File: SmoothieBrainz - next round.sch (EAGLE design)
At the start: 232 parts, among them IC1 LPC1769, IC7 74LVC1G04, Q1 BSL207SP, Q2 12MHz, SW1 SW_TACT_4P_B, SW3 SW_TACT_4P_B, T1 BC817, U3 USD-SOCKETUSD, X1 MSTBA2, X14 USBPTH, X2 GMSTBA2, X3 GMSTBA4, X4 1751248, X5 1751248, X6 1751248, X7 1751248

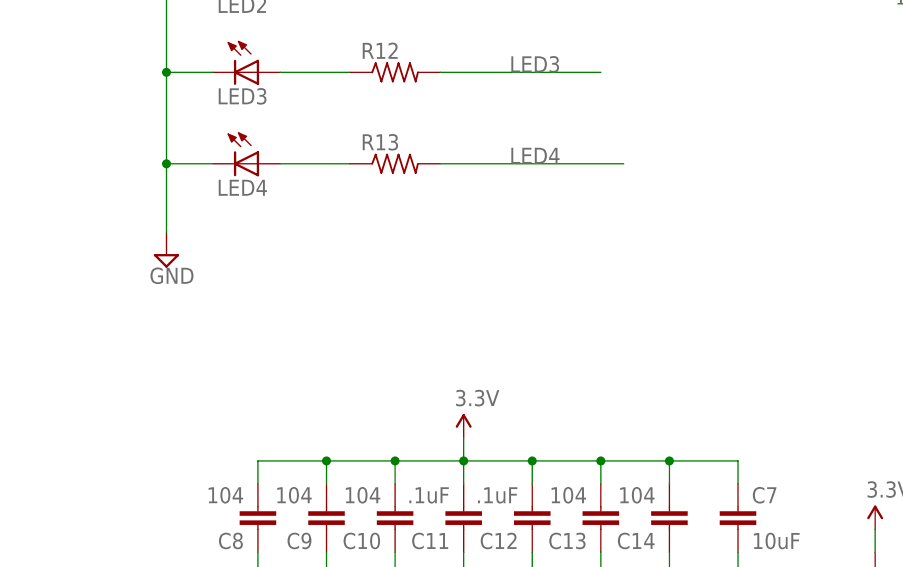
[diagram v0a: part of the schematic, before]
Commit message: Added VMOT indicator led
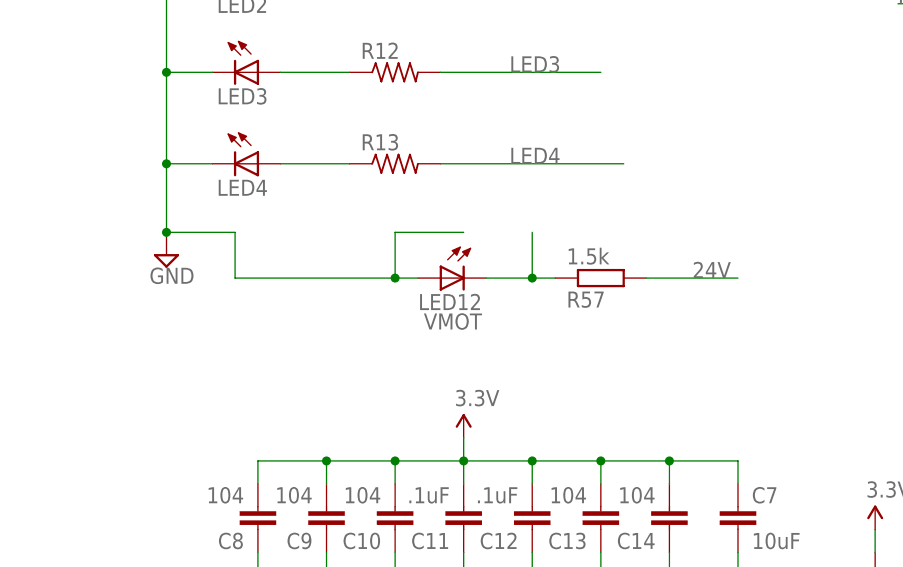
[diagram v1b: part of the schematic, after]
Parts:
- added LED12: VMOT, led:LEDSML0603
- added R57: 1.5k, resistor:R-EU_R0603
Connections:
- new net N$23: LED12.C, R57.1
- net 24V: now also R57.2
- net GND: now also LED12.A
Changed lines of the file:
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@@
 <part name="C23" library="resistor" deviceset="CPOL-EU" device="153CLV-0605" value="100u"/>
 <part name="C24" library="resistor" deviceset="CPOL-EU" device="153CLV-0605" value="100u"/>
+<part name="LED12" library="led" deviceset="LED" device="SML0603" value="VMOT"/>
+<part name="R57" library="resistor" deviceset="R-EU_" device="R0603" value="1.5k"/>
 </parts>
 <sheets>
@@
 <instance part="C23" gate="G$1" x="20.32" y="7.62"/>
 <instance part="C24" gate="G$1" x="68.58" y="7.62"/>
+<instance part="LED12" gate="G$1" x="43.18" y="73.66" rot="MR270"/>
+<instance part="R57" gate="G$1" x="60.96" y="73.66" rot="MR180"/>
 </instances>
 <busses>
@@
 <pinref part="LED3" gate="G$1" pin="C"/>
 <pinref part="LED4" gate="G$1" pin="C"/>
+<wire x1="12.7" y1="78.74" x2="20.32" y2="78.74" width="0.1524" layer="91"/>
+<wire x1="20.32" y1="78.74" x2="20.32" y2="73.66" width="0.1524" layer="91"/>
+<junction x="12.7" y="78.74"/>
+<pinref part="LED12" gate="G$1" pin="A"/>
+<wire x1="20.32" y1="73.66" x2="38.1" y2="73.66" width="0.1524" layer="91"/>
+<wire x1="38.1" y1="73.66" x2="40.64" y2="73.66" width="0.1524" layer="91"/>
+<wire x1="45.72" y1="78.74" x2="38.1" y2="78.74" width="0.1524" layer="91"/>
+<wire x1="38.1" y1="78.74" x2="38.1" y2="73.66" width="0.1524" layer="91"/>
+<junction x="38.1" y="73.66"/>
 </segment>
 <segment>
@@
 <label x="121.92" y="307.34" size="1.778" layer="95"/>
 </segment>
+<segment>
+<pinref part="R57" gate="G$1" pin="2"/>
+<wire x1="66.04" y1="73.66" x2="76.2" y2="73.66" width="0.1524" layer="91"/>
+<label x="71.12" y="73.66" size="1.778" layer="95"/>
+</segment>
 </net>
 <net name="N$16" class="0">
@@
 </segment>
 </net>
+<net name="N$23" class="0">
+<segment>
+<pinref part="R57" gate="G$1" pin="1"/>
+<pinref part="LED12" gate="G$1" pin="C"/>
+<wire x1="55.88" y1="73.66" x2="53.34" y2="73.66" width="0.1524" layer="91"/>
+<wire x1="53.34" y1="73.66" x2="48.26" y2="73.66" width="0.1524" layer="91"/>
+<wire x1="53.34" y1="78.74" x2="53.34" y2="73.66" width="0.1524" layer="91"/>
+<junction x="53.34" y="73.66"/>
+</segment>
+</net>

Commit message: More Cleanup.  Added Headers to Mosfet outputs
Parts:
- removed D13, D14, D5, D6: M4, semicon-smd-ipc:D-SOD-87
- removed R56: THERM, varistor:VARISTORCN0603
- removed SJ27: THERM-JUMPER, SparkFun-Retired:SOLDERJUMPERTRACE
- added JP16, JP21, JP22, JP23: (no value), SparkFun-Connectors:M02LOCK
- LED1, LED2, LED3, LED4, LED9: device led:LEDCHIP-LED0805 -> led:LEDSML0603
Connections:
- net AGND: no longer R56.1
- net E1-CONTROL: now also JP16.2; no longer D5.A
- net E2-CONTROL: now also JP21.2; no longer D6.A
- net E3-CONTROL: now also JP22.2; no longer D13.A
- net E4-CONTROL: now also JP23.2; no longer D14.A
- net HEATERVIN: now also JP16.1, JP21.1, JP22.1, JP23.1; no longer D13.C, D14.C, D5.C, D6.C
- net TH4: no longer R56.2, SJ27.1, SJ27.2

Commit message: rev2 initial ready
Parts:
- added D13, D14, D16, D4, D5, D6: 1N4148, SparkFun-DiscreteSemi:DIODEBAS16
- D10, D11, D12, D15, D7, D8, D9: value M4 -> 1N4148; device semicon-smd-ipc:D-SOD-87 -> SparkFun-DiscreteSemi:DIODEBAS16
- L1: value (none) -> 39nH
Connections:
- net 24V: now also D14.C
- net 5V: now also D16.C
- net E1-CONTROL: now also D4.A
- net E2-CONTROL: now also D5.A
- net E3-CONTROL: now also D6.A
- net E4-CONTROL: now also D13.A
- net HEATERVIN: now also D13.C, D4.C, D5.C, D6.C
- net N$56: now also D14.A, D16.A
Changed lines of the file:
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@@
 <part name="SUPPLY3" library="supply2" deviceset="GND" device=""/>
 <part name="C7" library="resistor" deviceset="C-EU" device="C0603" value="10uF"/>
-<part name="L1" library="SparkFun" deviceset="INDUCTOR" device="0603"/>
+<part name="L1" library="SparkFun" deviceset="INDUCTOR" device="0603" value="39nH"/>
 <part name="C6" library="rcl" deviceset="C-EU" device="C0603" value=".1uF"/>
 <part name="R14" library="resistor" deviceset="R-US_" device="R0603" value="10K"/>
@@
 <part name="EXP1" library="con-3m" deviceset="2510-" device=""/>
 <part name="EXP2" library="con-3m" deviceset="2510-" device=""/>
-<part name="D7" library="semicon-smd-ipc" deviceset="D-" device="SOD-87" value="M4"/>
-<part name="D8" library="semicon-smd-ipc" deviceset="D-" device="SOD-87" value="M4"/>
-<part name="D9" library="semicon-smd-ipc" deviceset="D-" device="SOD-87" value="M4"/>
-<part name="D10" library="semicon-smd-ipc" deviceset="D-" device="SOD-87" value="M4"/>
-<part name="D11" library="semicon-smd-ipc" deviceset="D-" device="SOD-87" value="M4"/>
-<part name="D12" library="semicon-smd-ipc" deviceset="D-" device="SOD-87" value="M4"/>
+<part name="D7" library="SparkFun-DiscreteSemi" deviceset="DIODE" device="BAS16" value="1N4148"/>
+<part name="D8" library="SparkFun-DiscreteSemi" deviceset="DIODE" device="BAS16" value="1N4148"/>
+<part name="D9" library="SparkFun-DiscreteSemi" deviceset="DIODE" device="BAS16" value="1N4148"/>
+<part name="D10" library="SparkFun-DiscreteSemi" deviceset="DIODE" device="BAS16" value="1N4148"/>
+<part name="D11" library="SparkFun-DiscreteSemi" deviceset="DIODE" device="BAS16" value="1N4148"/>
+<part name="D12" library="SparkFun-DiscreteSemi" deviceset="DIODE" device="BAS16" value="1N4148"/>
 <part name="R5" library="adafruit" deviceset="R-US_" device="R0603" value="10k"/>
 <part name="R6" library="adafruit" deviceset="R-US_" device="R0603" value="10k"/>
@@
 <part name="JP13" library="SparkFun-Connectors" deviceset="M03" device="LOCK"/>
 <part name="X1" library="con-phoenix-508" deviceset="MSTBA2" device=""/>
-<part name="D15" library="semicon-smd-ipc" deviceset="D-" device="SOD-87" value="M4"/>
+<part name="D15" library="SparkFun-DiscreteSemi" deviceset="DIODE" device="BAS16" value="1N4148"/>
 <part name="JP17" library="SparkFun-Connectors" deviceset="M08" device="LOCK"/>
 <part name="AGND4" library="supply1" deviceset="AGND" device=""/>
@@
 <part name="JP22" library="SparkFun-Connectors" deviceset="M02" device="LOCK"/>
 <part name="JP23" library="SparkFun-Connectors" deviceset="M02" device="LOCK"/>
+<part name="D4" library="SparkFun-DiscreteSemi" deviceset="DIODE" device="BAS16" value="1N4148"/>
+<part name="D5" library="SparkFun-DiscreteSemi" deviceset="DIODE" device="BAS16" value="1N4148"/>
+<part name="D6" library="SparkFun-DiscreteSemi" deviceset="DIODE" device="BAS16" value="1N4148"/>
+<part name="D13" library="SparkFun-DiscreteSemi" deviceset="DIODE" device="BAS16" value="1N4148"/>
+<part name="D14" library="SparkFun-DiscreteSemi" deviceset="DIODE" device="BAS16" value="1N4148"/>
+<part name="D16" library="SparkFun-DiscreteSemi" deviceset="DIODE" device="BAS16" value="1N4148"/>
 </parts>
 <sheets>
@@
 <instance part="JP22" gate="G$1" x="607.06" y="264.16" rot="R180"/>
 <instance part="JP23" gate="G$1" x="607.06" y="231.14" rot="R180"/>
+<instance part="D4" gate="G$1" x="551.18" y="325.12" rot="R180"/>
+<instance part="D5" gate="G$1" x="548.64" y="281.94" rot="R180"/>
+<instance part="D6" gate="G$1" x="548.64" y="248.92" rot="R180"/>
+<instance part="D13" gate="G$1" x="546.1" y="215.9" rot="R180"/>
+<instance part="D14" gate="G$1" x="515.62" y="152.4" rot="R90"/>
+<instance part="D16" gate="G$1" x="510.54" y="152.4" rot="R90"/>
 </instances>
 <busses>
@@
 <pinref part="GND4" gate="1" pin="GND"/>
 <pinref part="T1" gate="G$1" pin="E"/>
-<wire x1="518.16" y1="124.46" x2="518.16" y2="129.54" width="0.1524" layer="91"/>
 <pinref part="R55" gate="G$1" pin="1"/>
+<wire x1="518.16" y1="124.46" x2="518.16" y2="129.54" width="0.1524" layer="91"/>
 <wire x1="518.16" y1="129.54" x2="518.16" y2="132.08" width="0.1524" layer="91"/>
 <wire x1="515.62" y1="129.54" x2="518.16" y2="129.54" width="0.1524" layer="91"/>
@@
 <segment>
 <pinref part="JP13" gate="G$1" pin="3"/>
-<wire x1="535.94" y1="147.32" x2="525.78" y2="147.32" width="0.1524" layer="91"/>
+<wire x1="535.94" y1="147.32" x2="530.86" y2="147.32" width="0.1524" layer="91"/>
 <label x="525.78" y="144.78" size="1.778" layer="95"/>
+<pinref part="D16" gate="G$1" pin="C"/>
+<wire x1="530.86" y1="147.32" x2="525.78" y2="147.32" width="0.1524" layer="91"/>
+<wire x1="510.54" y1="154.94" x2="510.54" y2="160.02" width="0.1524" layer="91"/>
+<wire x1="510.54" y1="160.02" x2="530.86" y2="160.02" width="0.1524" layer="91"/>
+<wire x1="530.86" y1="160.02" x2="530.86" y2="147.32" width="0.1524" layer="91"/>
+<junction x="530.86" y="147.32"/>
 </segment>
 <segment>
@@
 <segment>
 <pinref part="JP13" gate="G$1" pin="1"/>
-<wire x1="535.94" y1="152.4" x2="525.78" y2="152.4" width="0.1524" layer="91"/>
 <label x="525.78" y="152.4" size="1.778" layer="95"/>
+<wire x1="535.94" y1="152.4" x2="533.4" y2="152.4" width="0.1524" layer="91"/>
+<pinref part="D14" gate="G$1" pin="C"/>
+<wire x1="533.4" y1="152.4" x2="525.78" y2="152.4" width="0.1524" layer="91"/>
+<wire x1="515.62" y1="154.94" x2="515.62" y2="157.48" width="0.1524" layer="91"/>
+<wire x1="515.62" y1="157.48" x2="533.4" y2="157.48" width="0.1524" layer="91"/>
+<wire x1="533.4" y1="157.48" x2="533.4" y2="152.4" width="0.1524" layer="91"/>
+<junction x="533.4" y="152.4"/>
 </segment>
 <segment>
@@
 <wire x1="599.44" y1="337.82" x2="556.26" y2="337.82" width="0.1524" layer="91"/>
 <wire x1="556.26" y1="337.82" x2="556.26" y2="335.28" width="0.1524" layer="91"/>
+<pinref part="D4" gate="G$1" pin="A"/>
 </segment>
 </net>
@@
 <wire x1="548.64" y1="325.12" x2="538.48" y2="325.12" width="0.1524" layer="91"/>
 <label x="533.4" y="325.12" size="1.778" layer="95"/>
+<pinref part="D4" gate="G$1" pin="C"/>
 </segment>
 <segment>
 <wire x1="546.1" y1="281.94" x2="535.94" y2="281.94" width="0.1524" layer="91"/>
 <label x="530.86" y="281.94" size="1.778" layer="95"/>
+<pinref part="D5" gate="G$1" pin="C"/>
 </segment>
 <segment>
 <wire x1="546.1" y1="248.92" x2="535.94" y2="248.92" width="0.1524" layer="91"/>
 <label x="530.86" y="248.92" size="1.778" layer="95"/>
+<pinref part="D6" gate="G$1" pin="C"/>
 </segment>
 <segment>
 <wire x1="543.56" y1="215.9" x2="533.4" y2="215.9" width="0.1524" layer="91"/>
 <label x="528.32" y="215.9" size="1.778" layer="95"/>
+<pinref part="D13" gate="G$1" pin="C"/>
 </segment>
 <segment>
@@
 <segment>
 <pinref part="T1" gate="G$1" pin="C"/>
-<wire x1="518.16" y1="142.24" x2="518.16" y2="144.78" width="0.1524" layer="91"/>
 <pinref part="JP13" gate="G$1" pin="2"/>
-<wire x1="518.16" y1="144.78" x2="518.16" y2="147.32" width="0.1524" layer="91"/>
+<wire x1="518.16" y1="142.24" x2="518.16" y2="149.86" width="0.1524" layer="91"/>
 <wire x1="535.94" y1="149.86" x2="518.16" y2="149.86" width="0.1524" layer="91"/>
-<wire x1="518.16" y1="149.86" x2="518.16" y2="147.32" width="0.1524" layer="91"/>
+<pinref part="D14" gate="G$1" pin="A"/>
+<wire x1="518.16" y1="149.86" x2="515.62" y2="149.86" width="0.1524" layer="91"/>
+<junction x="518.16" y="149.86"/>
+<pinref part="D16" gate="G$1" pin="A"/>
+<wire x1="515.62" y1="149.86" x2="510.54" y2="149.86" width="0.1524" layer="91"/>
+<junction x="515.62" y="149.86"/>
 </segment>
 </net>
@@
 <junction x="553.72" y="292.1"/>
 <wire x1="553.72" y1="294.64" x2="553.72" y2="292.1" width="0.1524" layer="91"/>
+<pinref part="D5" gate="G$1" pin="A"/>
 </segment>
 </net>
@@
 <junction x="553.72" y="259.08"/>
 <wire x1="553.72" y1="261.62" x2="553.72" y2="259.08" width="0.1524" layer="91"/>
+<pinref part="D6" gate="G$1" pin="A"/>
 </segment>
 </net>
@@
 <junction x="551.18" y="226.06"/>
 <wire x1="551.18" y1="228.6" x2="551.18" y2="226.06" width="0.1524" layer="91"/>
+<pinref part="D13" gate="G$1" pin="A"/>
 </segment>
 </net>
